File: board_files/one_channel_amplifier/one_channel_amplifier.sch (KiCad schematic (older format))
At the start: 22 parts, among them U1 LM3886

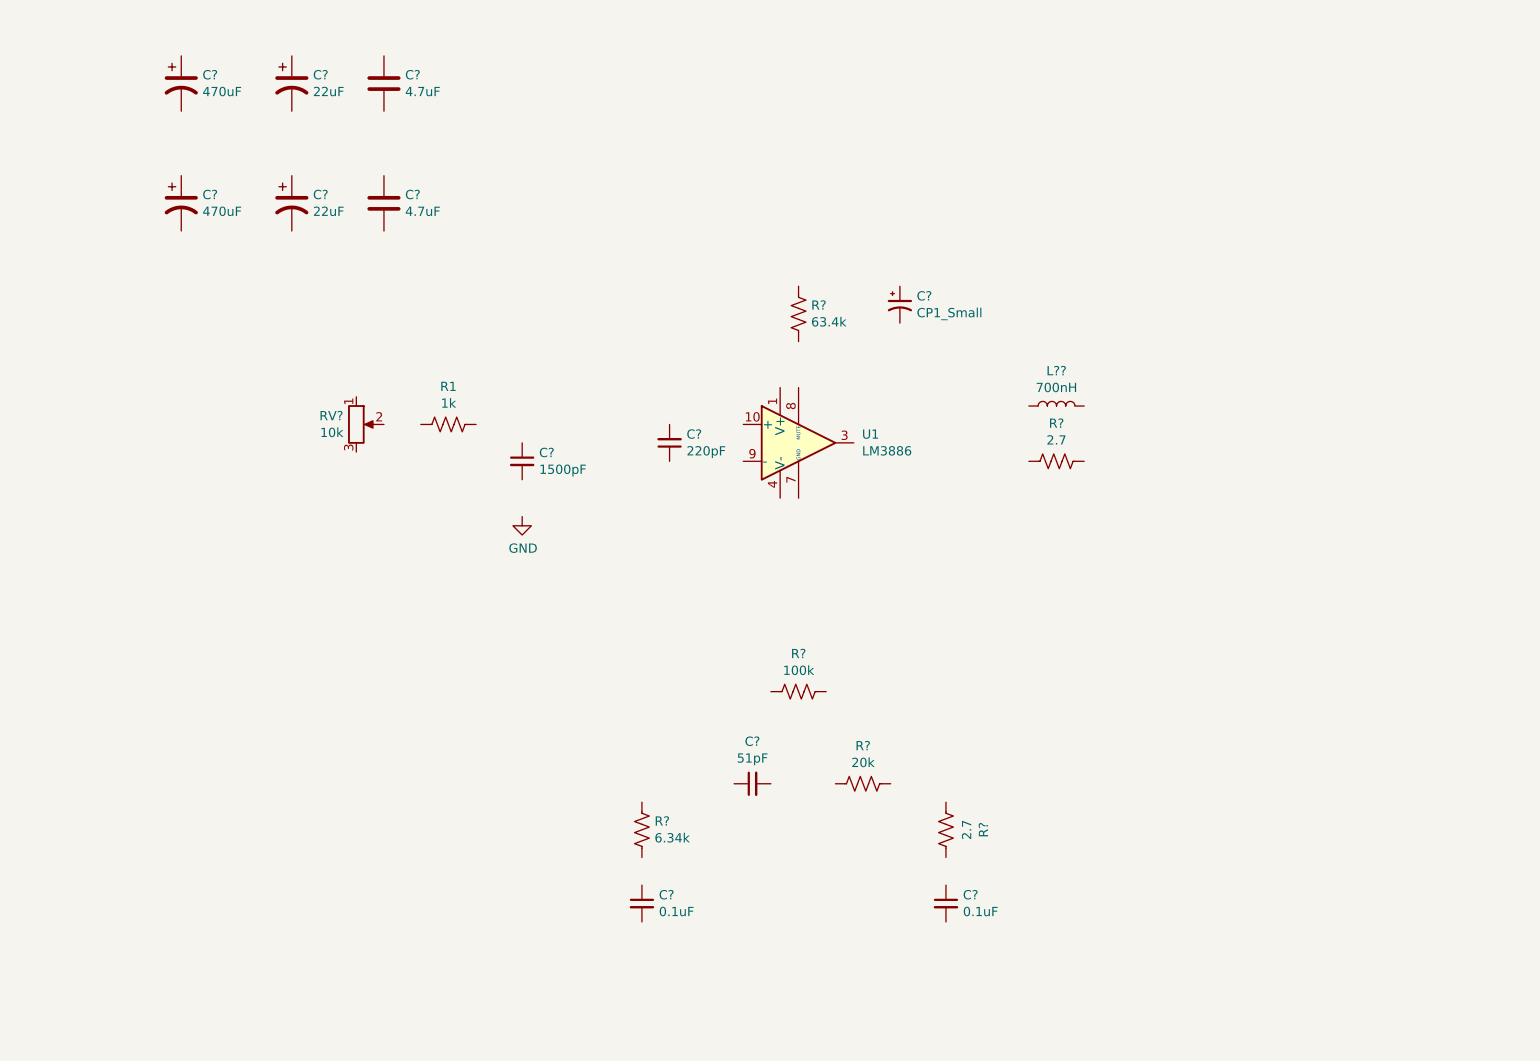
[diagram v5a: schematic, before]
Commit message: finished schematic, started panel BOM
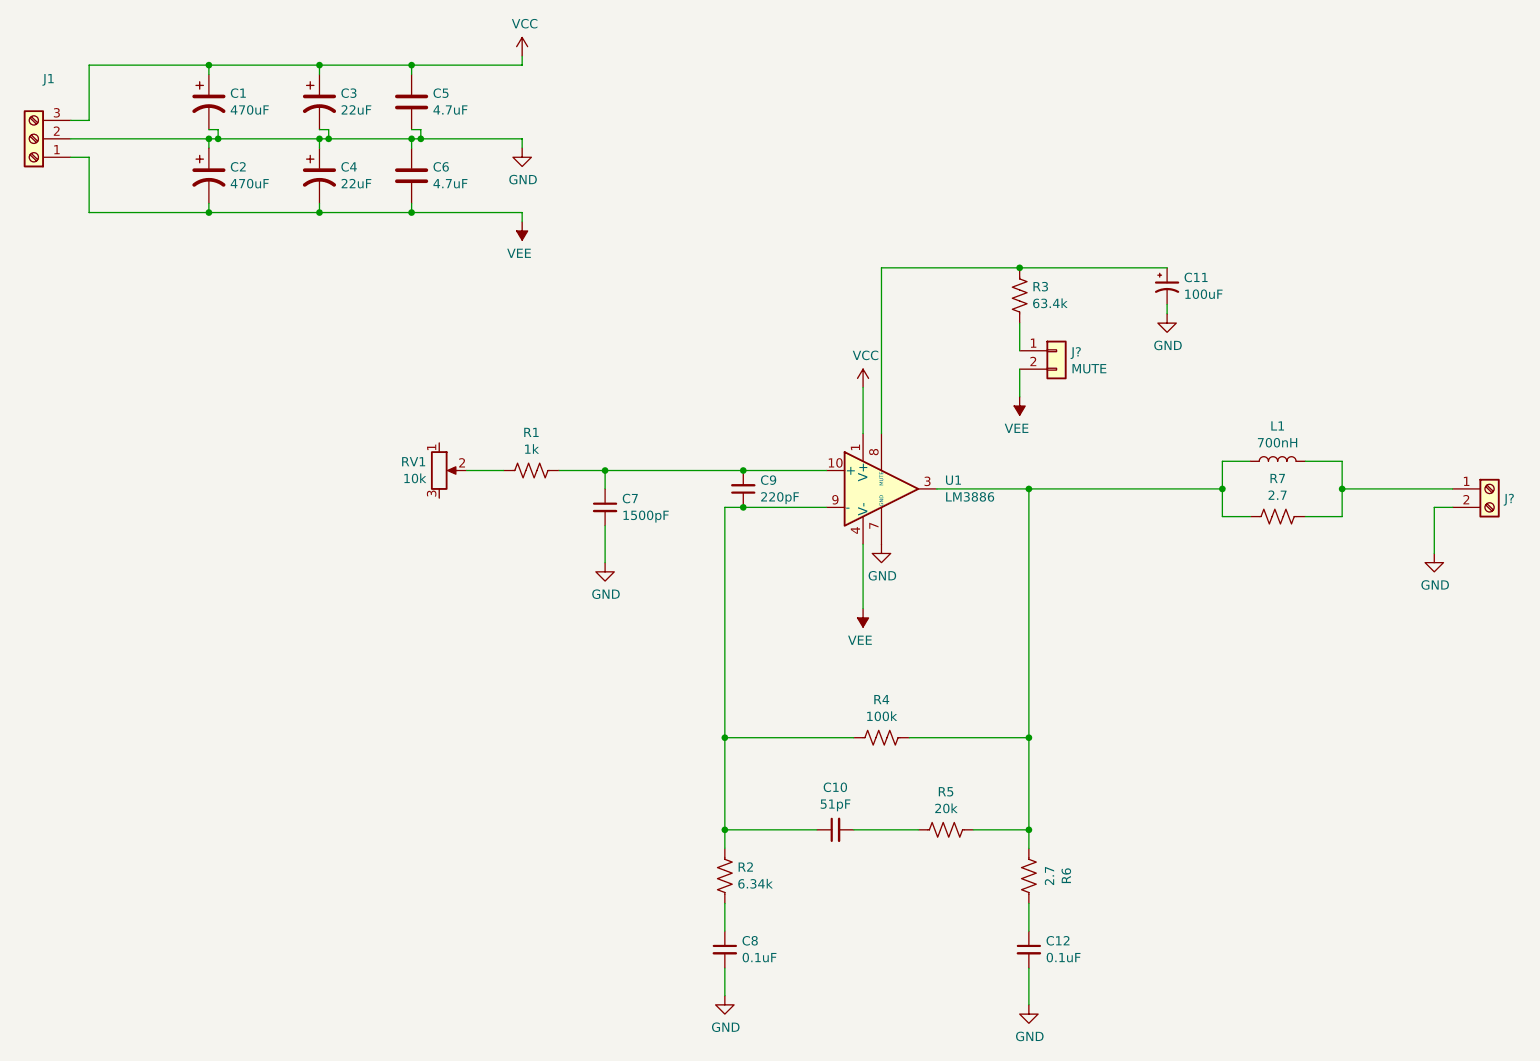
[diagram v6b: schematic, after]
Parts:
- removed R?: 2.7, Resistor_SMD:R_0805_2012Metric, symbol Device:R_US
- added J1: Screw_Terminal_01x03, TerminalBlock:TerminalBlock_bornier-3_P5.08mm, symbol Connector:Screw_Terminal_01x03
- added J?: Conn_01x02, symbol Connector_Generic:Conn_01x02
- added J?: Screw_Terminal_01x02, TerminalBlock:TerminalBlock_bornier-2_P5.08mm, symbol Connector:Screw_Terminal_01x02
- added R6: 2.7, Resistor_SMD:R_0603_1608Metric, symbol Device:R_US
- C11: renamed from C?; value CP1_Small -> 100uF; footprint (none) -> Capacitor_THT:CP_Radial_D8.0mm_P3.50mm; Description (none) -> CAP ALUM 100UF 20% 50V RADIAL; MPN (none) -> ECA-1HM101
- C7: renamed from C?; footprint Capacitor_SMD:C_0805_2012Metric -> Capacitor_SMD:C_0603_1608Metric; Description CAP CER 1500PF 50V X7R 0805 -> CAP CER 1500PF 100V X7R 0603; Digikey PN (none) -> 490-1475-1-ND; MPN 885012207087 -> GRM188R72A152KA01D
- C9: renamed from C?; footprint Capacitor_SMD:C_0805_2012Metric -> Capacitor_SMD:C_0603_1608Metric; Description CAP CER 220PF 10V X7R 0805 -> CAP CER 220PF 100V X7R 0603; Digikey PN (none) -> 399-7877-1-ND; MPN 885012207005 -> C0603C221K1RACTU
- L1: renamed from L??; MPN (none) -> PA0277NL
- R1: footprint Resistor_SMD:R_0805_2012Metric -> Resistor_SMD:R_0603_1608Metric; Description RES 1K OHM 1% 1/8W 0805 -> RES SMD 1K OHM 1% 1/10W 0603; Digikey PN (none) -> 311-1.00KHRCT-ND; MPN CRCW08051K00FKEAC -> RC0603FR-071KL
- R2: renamed from R?; footprint Capacitor_SMD:C_0805_2012Metric -> Resistor_SMD:R_0603_1608Metric; Description RES SMD 6.34K OHM 1% 1/8W 0805 -> RES SMD 6.34K OHM 1% 1/10W 0603
- R3: renamed from R?; footprint Resistor_SMD:R_0805_2012Metric -> Resistor_SMD:R_0603_1608Metric; Description RES SMD 63.4K OHM 1% 1/8W 0805 -> RES SMD 63.4K OHM 1% 1/10W 0603; MPN ERJ-6ENF6342V -> ERJ-3EKF6342V
- R4: renamed from R?; footprint Resistor_SMD:R_0805_2012Metric -> Resistor_SMD:R_0603_1608Metric; Description RES SMD 100K OHM 1% 1/8W 0805 -> RES 100K OHM 1% 1/10W 0603; MPN RC0805FR-07100KL -> RMCF0603FT100K
- R7: renamed from R?; footprint Resistor_SMD:R_0805_2012Metric -> Resistor_SMD:R_0603_1608Metric; Description RES 2.7 OHM 1% 1/4W 0805 -> RES 2.7 OHM 1% 1/8W 0603; Digikey PN (none) -> 2019-RK73H1JTTD2R70FCT-ND; MPN RK73H2ATTD2R70F -> RK73H1JTTD2R70F
- gave numbers to parts that had none: 11
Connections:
- net GND: now also C1.2, C11.2, C12.2, C2.1, C3.2, C4.1, C5.2, C6.1, C7.2, C8.2, U1.7 (GND), J1.2 (Pin_2), J?.2 (Pin_2)
- net VCC: now reaches U1.1 (V+), U1.5 (V+)
- net VCC: now also C1.1, C3.1, C5.1, J1.3 (Pin_3)
- net at U1.10 (+): now also C7.1, C9.2, R1.1
- net at U1.3: now also L1.1, R4.1, R5.1, R7.1, R6.1
- net VEE: now reaches U1.4 (V-)
- net VEE: now also C2.2, C4.2, C6.2, J1.1 (Pin_1), J?.2 (Pin_2)
- net at U1.8 (MUTE): now also C11.1, R3.1
- net at U1.9 (-): now also C10.1, C9.1, R2.1, R4.2
- net at R1.2: now also RV1.2
- net at R7.2: now also L1.2, J?.1 (Pin_1)
- net at R3.2: now also J?.1 (Pin_1)
- net at C12.1: now also R6.2
- net at R2.2: now also C8.1
- net at R5.2: now also C10.2
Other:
- moved on the sheet: C1, C10, C11, C12, C2, C3, C4, C5, C6, C7, C8, C9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

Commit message: Finalized sch and exported to layout
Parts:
- removed RV1: 10k, Potentiometer_THT:Potentiometer_Bourns_3386P_Vertical, symbol Device:R_POT
- added J2: Conn_01x02, Connector_PinHeader_2.54mm:PinHeader_1x02_P2.54mm_Vertical, symbol Connector_Generic:Conn_01x02
- J3: renamed from J?; footprint (none) -> Connector_PinHeader_2.54mm:PinHeader_1x02_P2.54mm_Vertical
- gave numbers to parts that had none: 1
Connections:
- net GND: now also J2.1 (Pin_1)
- net at R1.2: now also J2.2 (Pin_2)
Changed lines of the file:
@@
-$EndComp
-$Comp
-L Device:R_POT RV1
-U 1 1 5EE0D429
-P 3050 3250
-F 0 "RV1" H 2980 3296 50  0000 R CNN
-F 1 "10k" H 2980 3205 50  0000 R CNN
-F 2 "Potentiometer_THT:Potentiometer_Bourns_3386P_Vertical" H 3050 3250 50  0001 C CNN
-F 3 "~" H 3050 3250 50  0001 C CNN
-F 4 "POT 10K OHM 1/5W PLASTIC LINEAR" H 3050 3250 50  0001 C CNN "Description"
-F 5 "P160KN-0QD15B10K" H 3050 3250 50  0001 C CNN "MPN"
-	1    3050 3250
-	1    0    0    -1
 $EndComp
 $Comp
@@
 Connection ~ 1800 1850
 $Comp
-L power:GND #PWR?
+L power:GND #PWR010
 U 1 1 5EEA34EE
 P 5450 3650
-F 0 "#PWR?" H 5450 3400 50  0001 C CNN
+F 0 "#PWR010" H 5450 3400 50  0001 C CNN
 F 1 "GND" H 5455 3477 50  0000 C CNN
 F 2 "" H 5450 3650 50  0001 C CNN
@@
 	2900 1850 3500 1850
 $Comp
-L power:VEE #PWR?
+L power:VEE #PWR09
 U 1 1 5EEA5198
 P 5350 4000
-F 0 "#PWR?" H 5350 3850 50  0001 C CNN
+F 0 "#PWR09" H 5350 3850 50  0001 C CNN
 F 1 "VEE" H 5365 4173 50  0000 C CNN
 F 2 "" H 5350 4000 50  0001 C CNN
@@
 $EndComp
 $Comp
-L power:GND #PWR?
+L power:GND #PWR07
 U 1 1 5EEA6A0D
 P 4600 6100
-F 0 "#PWR?" H 4600 5850 50  0001 C CNN
+F 0 "#PWR07" H 4600 5850 50  0001 C CNN
 F 1 "GND" H 4605 5927 50  0000 C CNN
 F 2 "" H 4600 6100 50  0001 C CNN
@@
 $EndComp
 $Comp
-L power:GND #PWR?
+L power:GND #PWR012
 U 1 1 5EEA71FD
 P 6250 6150
-F 0 "#PWR?" H 6250 5900 50  0001 C CNN
+F 0 "#PWR012" H 6250 5900 50  0001 C CNN
 F 1 "GND" H 6255 5977 50  0000 C CNN
 F 2 "" H 6250 6150 50  0001 C CNN
@@
 $EndComp
 $Comp
-L power:VCC #PWR?
+L power:VCC #PWR08
 U 1 1 5EEAB19F
 P 5350 2800
-F 0 "#PWR?" H 5350 2650 50  0001 C CNN
+F 0 "#PWR08" H 5350 2650 50  0001 C CNN
 F 1 "VCC" H 5365 2973 50  0000 C CNN
 F 2 "" H 5350 2800 50  0001 C CNN
@@
 	3950 3250 4700 3250
 Wire Wire Line
-	3400 3250 3200 3250
-Wire Wire Line
 	3950 3750 3950 3550
 $Comp
-L Connector_Generic:Conn_01x02 J?
+L Connector_Generic:Conn_01x02 J3
 U 1 1 5EEB4E0E
 P 6400 2600
-F 0 "J?" H 6480 2592 50  0000 L CNN
+F 0 "J3" H 6480 2592 50  0000 L CNN
 F 1 "Conn_01x02" H 6480 2501 50  0001 L CNN
-F 2 "" H 6400 2600 50  0001 C CNN
+F 2 "Connector_PinHeader_2.54mm:PinHeader_1x02_P2.54mm_Vertical" H 6400 2600 50  0001 C CNN
 F 3 "~" H 6400 2600 50  0001 C CNN
 F 4 "MUTE" H 6480 2501 50  0000 L CNN "Description"
@@
 $EndComp
 $Comp
-L power:VEE #PWR?
+L power:VEE #PWR011
 U 1 1 5EEB7168
 P 6200 2850
-F 0 "#PWR?" H 6200 2700 50  0001 C CNN
+F 0 "#PWR011" H 6200 2700 50  0001 C CNN
 F 1 "VEE" H 6215 3023 50  0000 C CNN
 F 2 "" H 6200 2850 50  0001 C CNN
@@
 	6200 2600 6200 2450
 $Comp
-L power:GND #PWR?
+L power:GND #PWR013
 U 1 1 5EEC325C
 P 7000 2400
-F 0 "#PWR?" H 7000 2150 50  0001 C CNN
+F 0 "#PWR013" H 7000 2150 50  0001 C CNN
 F 1 "GND" H 7005 2227 50  0000 C CNN
 F 2 "" H 7000 2400 50  0001 C CNN
@@
 	7950 3500 7750 3500
 $Comp
-L Connector:Screw_Terminal_01x02 J?
+L Connector:Screw_Terminal_01x02 J4
 U 1 1 5EEC8473
 P 8750 3350
-F 0 "J?" H 8830 3296 50  0000 L CNN
+F 0 "J4" H 8830 3296 50  0000 L CNN
 F 1 "Screw_Terminal_01x02" H 8830 3251 50  0001 L CNN
 F 2 "TerminalBlock:TerminalBlock_bornier-2_P5.08mm" H 8750 3350 50  0001 C CNN
@@
 $EndComp
 $Comp
-L power:GND #PWR?
+L power:GND #PWR014
 U 1 1 5EECA5F4
 P 8450 3700
-F 0 "#PWR?" H 8450 3450 50  0001 C CNN
+F 0 "#PWR014" H 8450 3450 50  0001 C CNN
 F 1 "GND" H 8455 3527 50  0000 C CNN
 F 2 "" H 8450 3700 50  0001 C CNN
@@
 Wire Wire Line
 	5350 3650 5350 4000
+$Comp
+L power:GND #PWR05
+U 1 1 5EE9133A
+P 1150 3550
+F 0 "#PWR05" H 1150 3300 50  0001 C CNN
+F 1 "GND" H 1155 3377 50  0000 C CNN
+F 2 "" H 1150 3550 50  0001 C CNN
+F 3 "" H 1150 3550 50  0001 C CNN
+	1    1150 3550
+	1    0    0    -1
+$EndComp
+Wire Wire Line
+	1150 3350 1150 3550
+$Comp
+L Connector_Generic:Conn_01x02 J2
+U 1 1 5EE87483
+P 800 3350
+F 0 "J2" H 718 3117 50  0000 C CNN
+F 1 "Conn_01x02" H 718 3116 50  0001 C CNN
+F 2 "Connector_PinHeader_2.54mm:PinHeader_1x02_P2.54mm_Vertical" H 800 3350 50  0001 C CNN
+F 3 "~" H 800 3350 50  0001 C CNN
+	1    800  3350
+	-1   0    0    1
+$EndComp
+Wire Wire Line
+	1150 3350 1000 3350
+Wire Wire Line
+	1000 3250 3400 3250
 $EndSCHEMATC

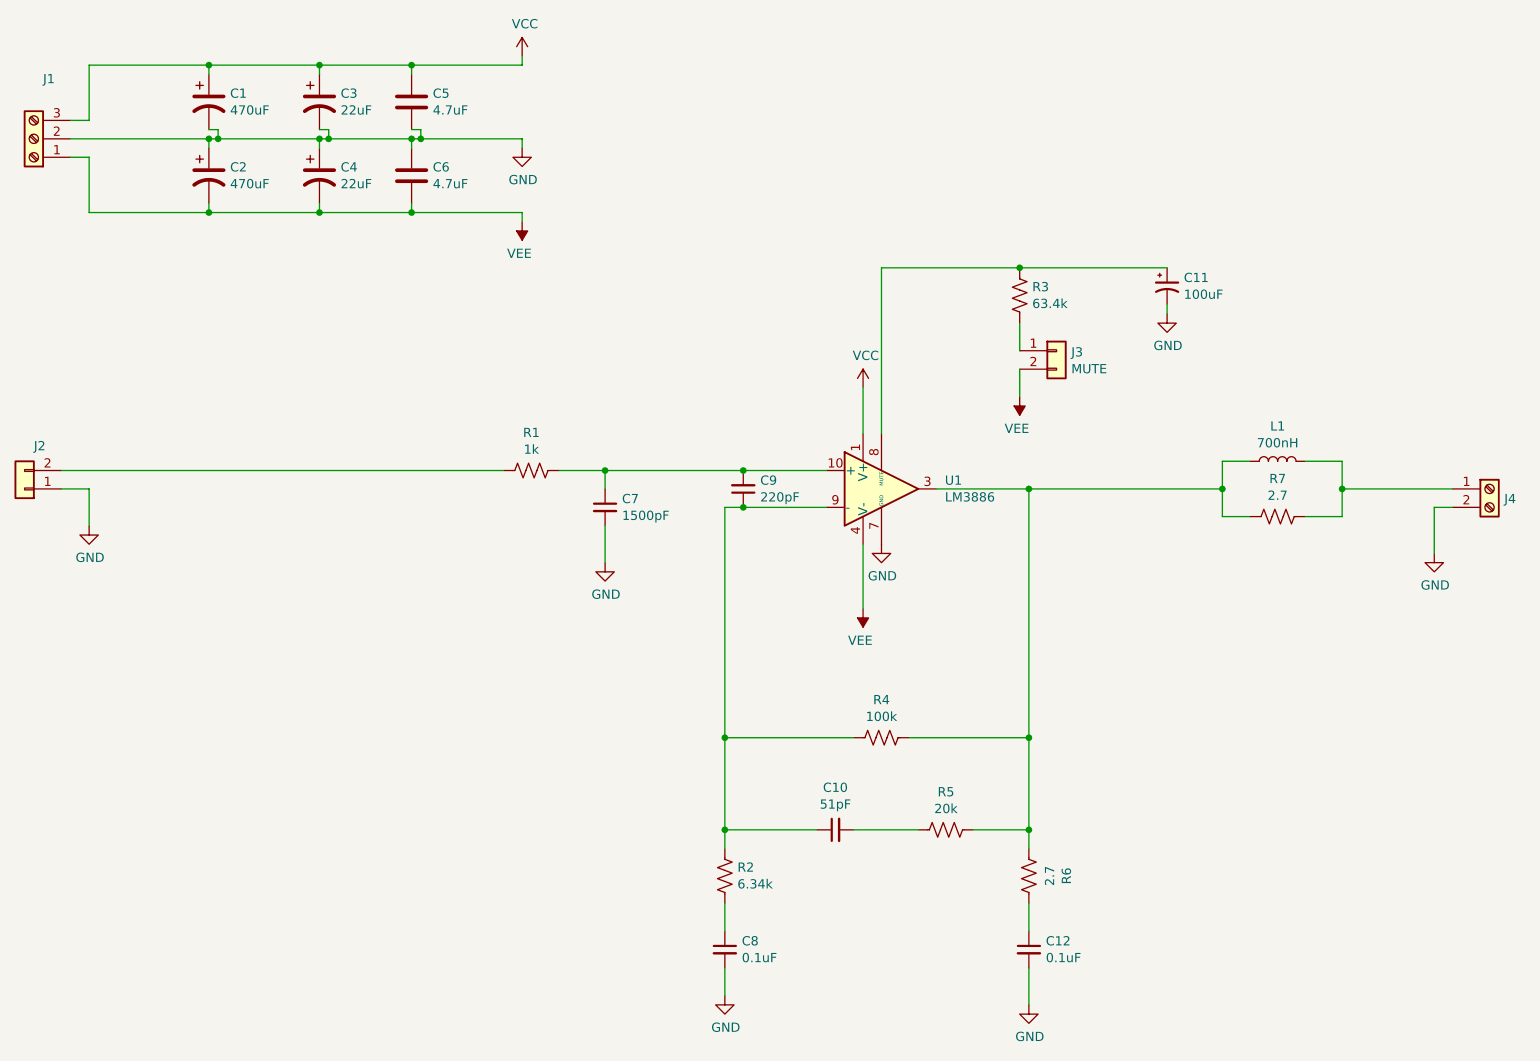
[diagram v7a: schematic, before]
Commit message: Changed power input to use quick connect plugs
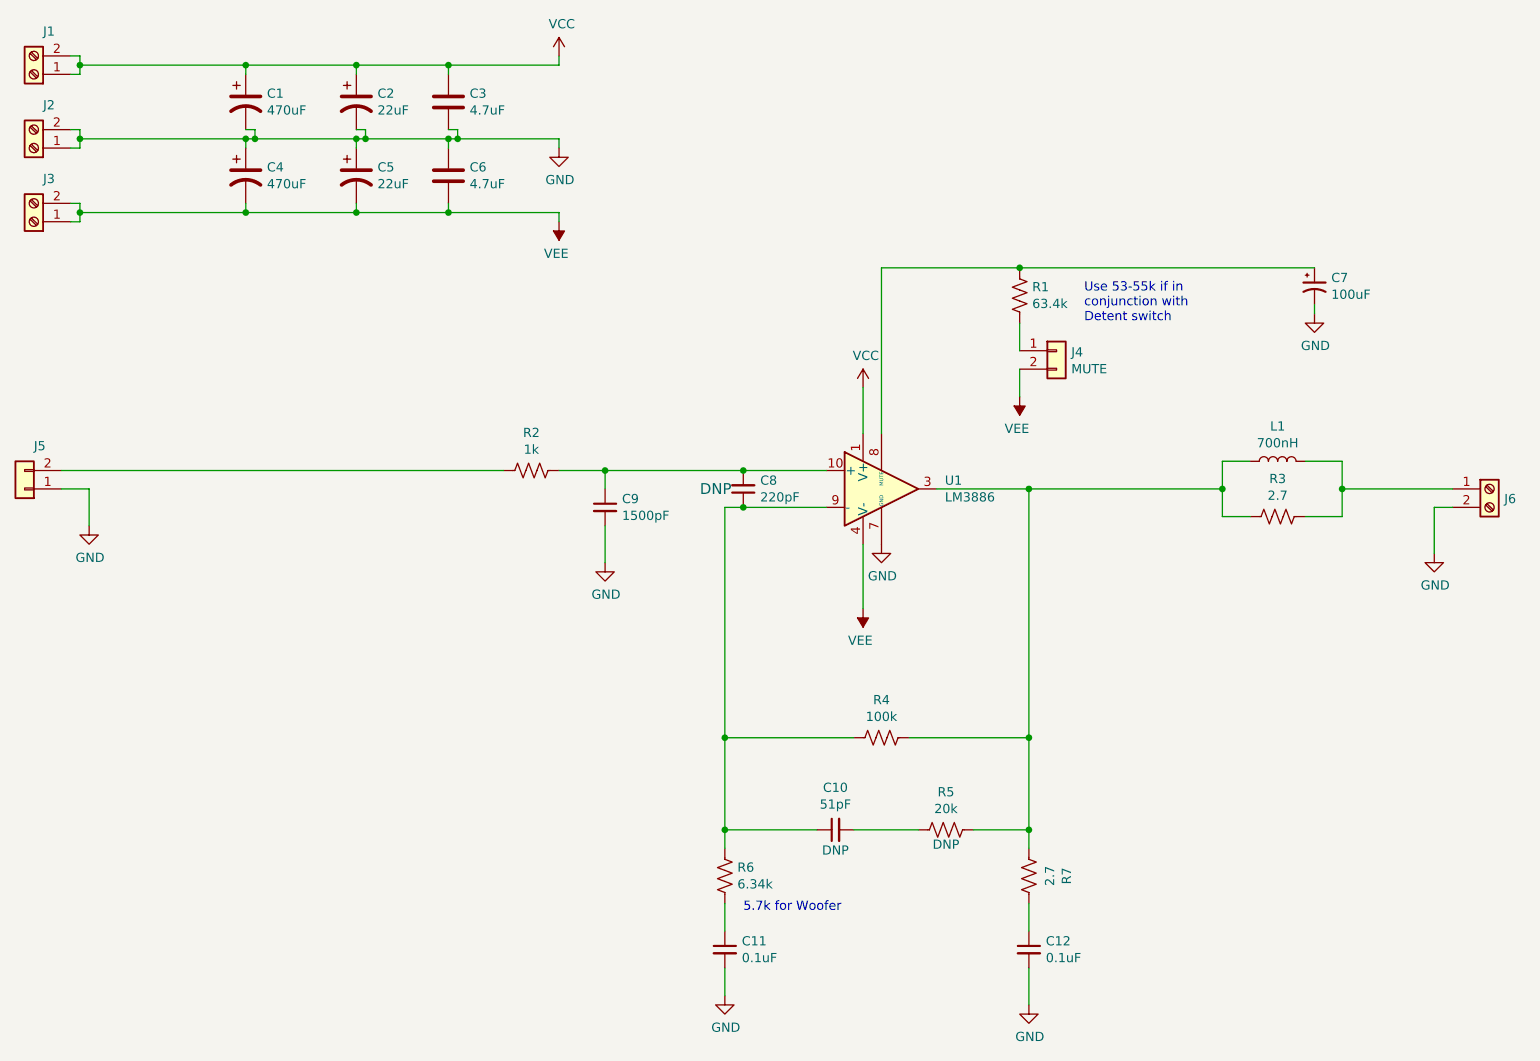
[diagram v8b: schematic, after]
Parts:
- removed J1: Screw_Terminal_01x03, TerminalBlock:TerminalBlock_bornier-3_P5.08mm, symbol Connector:Screw_Terminal_01x03
- added J1, J2, J3: Screw_Terminal_01x02, Connector_QC_Blade_User:TE_QC_250_Male_Blade_P5.08, symbol Connector:Screw_Terminal_01x02
- C10, R5: Stuffing (none) -> DNP
- C8: renamed from C9; Stuffing (none) -> DNP
- renumbered C8 to C11, C3 to C2, C5 to C3, C2 to C4, C4 to C5, C11 to C7, C7 to C9, J3 to J4, J2 to J5, J4 to J6, R3 to R1, R1 to R2, R7 to R3, R2 to R6, R6 to R7
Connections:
- net GND: now also J2.1 (Pin_1), J2.2 (Pin_2)
- net VCC: now also J1.1 (Pin_1), J1.2 (Pin_2)
- net VEE: now also J3.1 (Pin_1), J3.2 (Pin_2)
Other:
- note added: "5.7k for Woofer\n"
- note added: "Use 53-55k if in \nconjunction with \nDetent switch\n"
- moved on the sheet: C1, C2, C3, C4, C5, C6, C7
